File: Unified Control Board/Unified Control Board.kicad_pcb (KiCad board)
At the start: 4 copper layers, 101.6 x 120.8 mm, 172 parts, among them CN1 B02B-PASK(LF)(SN), CN10 B3B-XH-2(LF)(SN), CN11 B3B-XH-2(LF)(SN), CN2 B02B-PASK(LF)(SN), CN3 B02B-PASK(LF)(SN), CN4 B04B-PASK(LF)(SN), CN5 B04B-PASK(LF)(SN), CN6 B02B-PASK(LF)(SN), CN7 B04B-PASK(LF)(SN), CN8 B04B-PASK(LF)(SN), CN9 B3B-XH-2(LF)(SN), SW1 TSA002A3512A02, SW2 TSA002A3512A02, SW3 TSA002A3512A02, U1 XT60PB-M.G.Y, U10 2.4GHz, U11 MP6541A, U12 MP6541A, U2 DRV8876PWPR, U3 DRV8876PWPR, U4 DRV8876PWPR, U5 DRV8876PWPR, U6 TCA9546A, U7 ZDSD01GLGEAG, U8 ESP32-S3-WROOM-1, U9 AP64350SP-13

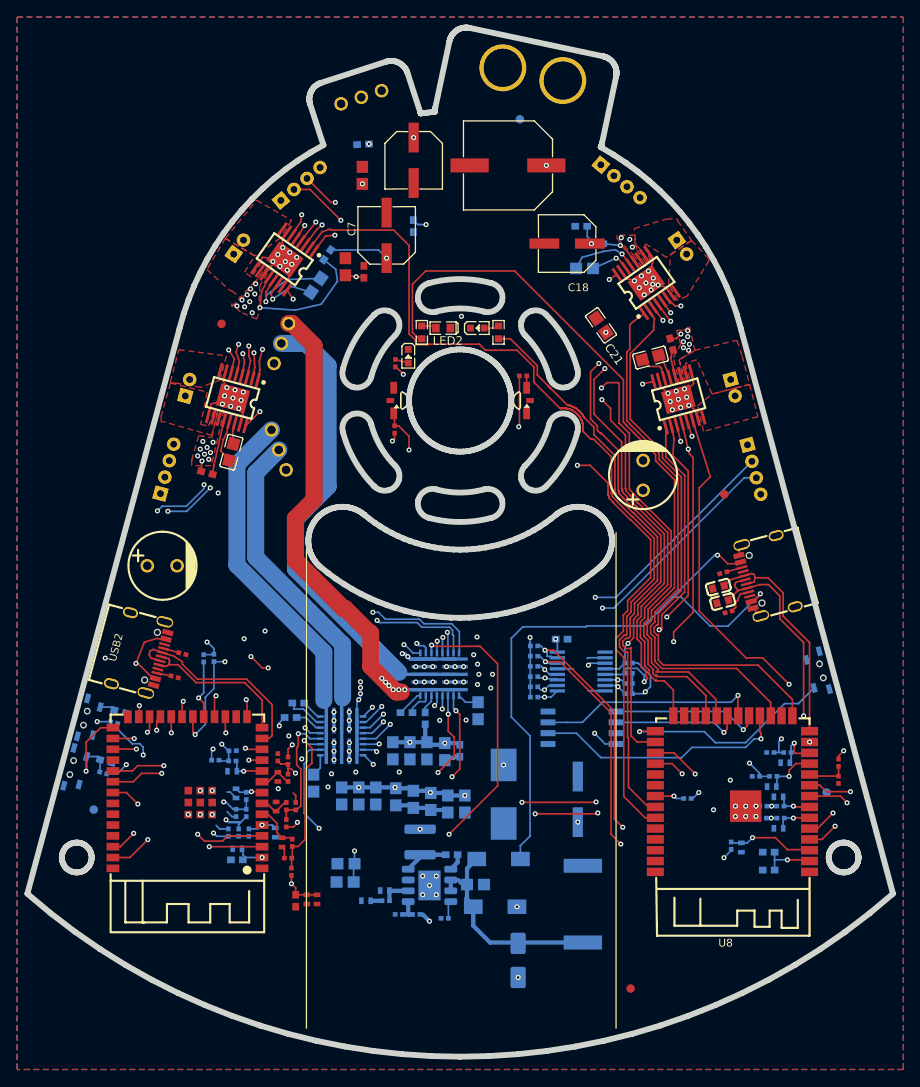
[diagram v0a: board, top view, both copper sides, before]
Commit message: Baseline: uncommitted 24V design state from working tree (C28 pad fix, BOM merge, regenerated fab outputs)
Captures the edits made after 500dc69 so the 36V changes that follow
are reviewable on their own.

Co-Authored-By: Claude Opus 5.5 <noreply@anthropic.com>
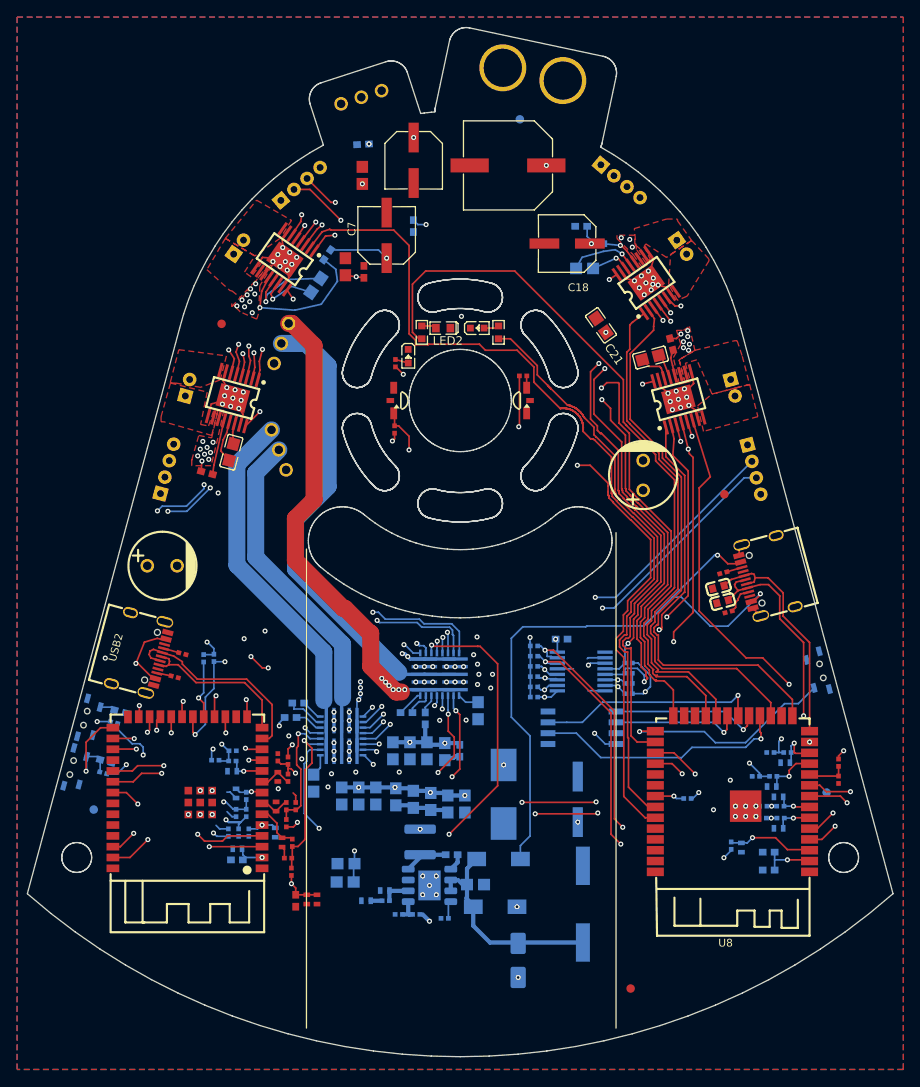
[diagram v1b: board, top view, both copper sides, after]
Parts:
- C56, C63: value 22uF/16V -> 22uF
- U10: value 2.4GHz -> ESP32-S3-WROOM-1
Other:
- outline, holes or cut-outs redrawn
